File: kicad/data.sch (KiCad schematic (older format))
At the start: 46 parts, among them J2 USB_C, J3 XCVR_CAT_TTL, J4 FTDI header, J5 PTT choice, J6 XCVR_PTT, J7 XCVR_CAT_RS232, U3 SN65220, U4 Si8663AB-B-IS1, U5 FT232RL, U6 MAX3387ECUG+, U7 VOR1121B6T

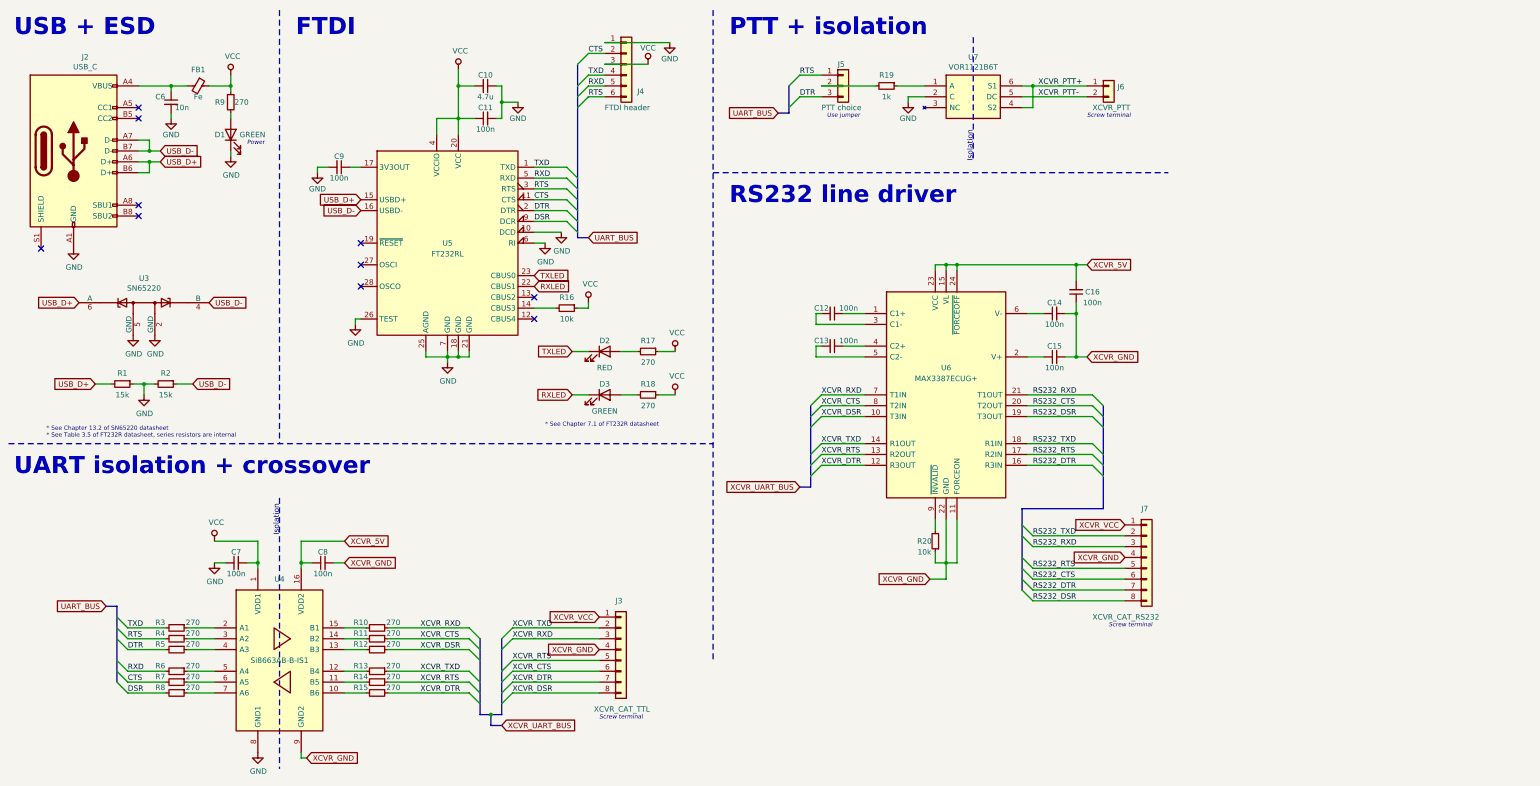
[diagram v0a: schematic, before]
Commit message: Filtering, jumpers, LEDs, misc
* Modified high level diagram to express the shared UART bus
* Renamed XCVR_VCC to XCVR_13V8
* Add solder jumpers on audio, PTT and UART lines for easy prototyping/bypassing
* Added bypass caps on XCVR side data and audio connectors
* Add series ferite beads on data ICs Vcc
* Added schottky diodes to all XCVR_13V8
* Changed series resistors of RXLED/TXLED/VccLED for 6mA current
* Added power LEDs on XCVR_13V8 connector terminals
* Added power LED for XCVR_5V rail
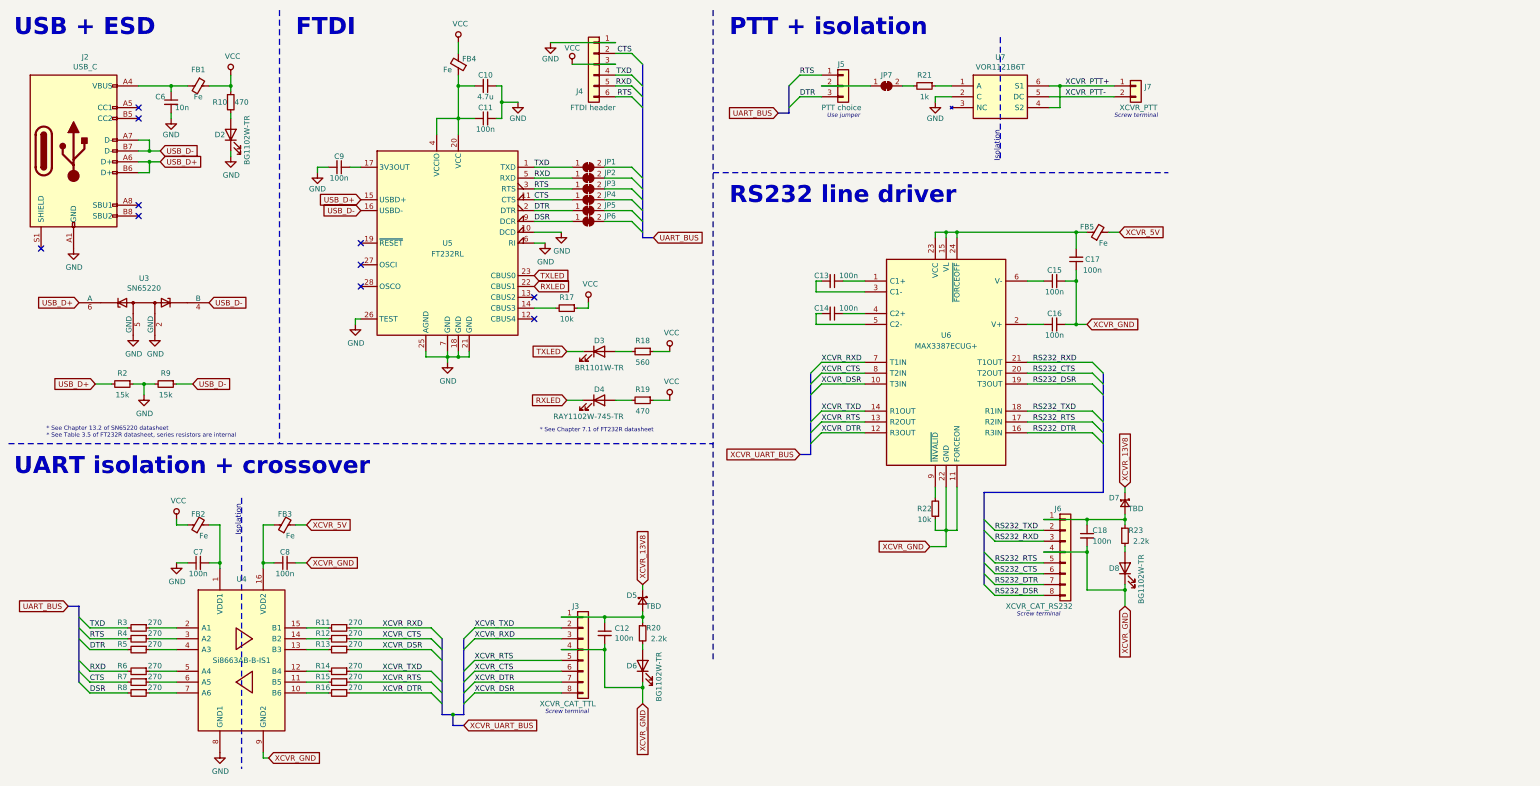
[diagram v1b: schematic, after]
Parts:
- added C12, C18: 100n, symbol Device:C_Small
- added D5, D7: TBD, symbol Device:D_Schottky_Small
- added D6, D8: BG1102W-TR, symbol Device:LED
- added FB2, FB3, FB4, FB5: Fe, symbol Device:Ferrite_Bead_Small
- added JP1, JP2, JP3, JP4, JP5, JP6, JP7: SolderJumper_2_Bridged, symbol Jumper:SolderJumper_2_Bridged
- added R20, R23: 2.2k, symbol Device:R_Small
- D2: renamed from D1; value GREEN -> BG1102W-TR
- D3: renamed from D2; value RED -> BR1101W-TR
- D4: renamed from D3; value GREEN -> RAY1102W-745-TR
- R10: renamed from R9; value 270 -> 470
- R18: renamed from R17; value 270 -> 560
- R19: renamed from R18; value 270 -> 470
- renumbered C12 to C13, C13 to C14, C14 to C15, C15 to C16, C16 to C17, J7 to J6, J6 to J7, R10 to R11, R11 to R12, R12 to R13, R13 to R14, R14 to R15, R15 to R16, R16 to R17, R1 to R2, R19 to R21, R20 to R22, R2 to R9
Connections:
- net CTS: now also JP4.1 (A)
- net DSR: now also JP6.1 (A)
- net DTR: now also JP5.1 (A)
- net RTS: now also JP3.1 (A)
- net RXD: now also JP2.1 (A)
- net TXD: now also JP1.1 (A)
- net VCC: now also FB2.1, FB4.2; no longer C10.2, C11.1, C7.2, U4.1 (VDD1), U5.20 (VCC), U5.4 (VCCIO)
- net XCVR_5V: now also FB3.2, FB5.2; no longer C17.2, C8.1, U4.16 (VDD2), U6.15 (VL), U6.23 (VCC), U6.24 (~FORCEOFF)
- net XCVR_GND: now also C12.2, C18.2, D6.1 (K), D8.1 (K)
- net at J5.2 (Pin_2): now also JP7.1 (A); no longer R21.2
- net XCVR_VCC: no longer names the net of J6.1 (Pin_1)
- net XCVR_VCC: now also C18.1, D7.2 (A), R23.1; no longer J3.1 (Pin_1)
- new net: C10.2, C11.1, FB4.1, U5.20 (VCC), U5.4 (VCCIO)
- new net: C12.1, D5.2 (A), J3.1 (Pin_1), R20.1
- new net: JP7.2 (B), R21.2
- new net: C17.2, FB5.1, U6.15 (VL), U6.23 (VCC), U6.24 (~FORCEOFF)
- new net: C7.2, FB2.2, U4.1 (VDD1)
- new net: C8.1, FB3.1, U4.16 (VDD2)
- new net: D8.2 (A), R23.2
- new net: D6.2 (A), R20.2
- new net XCVR_13V8: D5.1 (K), D7.1 (K)
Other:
- note removed: "Power"
- moved on the sheet: C13, C14, C15, C16, C17, C7, C8, D3, D4, J3, J4, J6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

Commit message: MAX driver protection
* Adjust label position for readability
* Protected R1OUT-R3OUT of MAX driver with OR gate
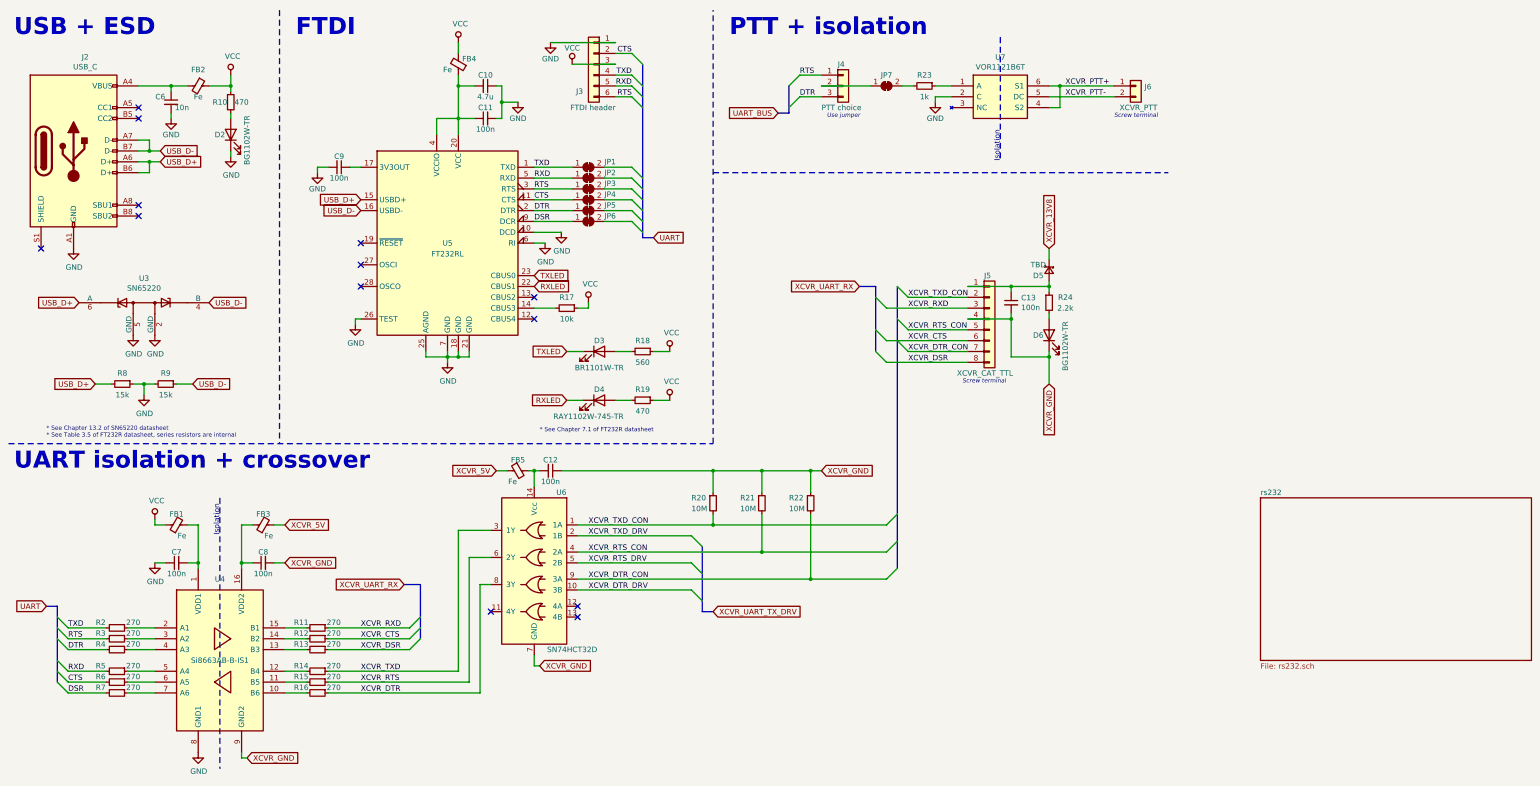
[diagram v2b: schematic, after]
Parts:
- removed C13, C14, C15, C16, C17, C18: 100n, symbol Device:C_Small
- removed D7: TBD, symbol Device:D_Schottky_Small
- removed D8: BG1102W-TR, symbol Device:LED
- removed J6: XCVR_CAT_RS232, symbol Connector_Generic:Conn_01x08
- removed R23: 2.2k, symbol Device:R_Small
- removed U6: MAX3387ECUG+, SOP65P640X110-24N, symbol custom:MAX3387ECUG+
- added C12: 100n, symbol Device:C_Small
- added R20, R21: 10M, symbol Device:R_Small
- added U6: SN74HCT32D, Package_SO:SOIC-14_3.9x8.7mm_P1.27mm, symbol custom:SN74HCT32D
- R22: value 10k -> 10M
- renumbered C12 to C13, FB2 to FB1, FB1 to FB2, J4 to J3, J5 to J4, J3 to J5, J7 to J6, R3 to R2, R21 to R23, R20 to R24, R4 to R3, R5 to R4, R6 to R5, R7 to R6, R8 to R7, R2 to R8
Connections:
- net XCVR_5V: now also FB5.1; no longer FB5.2
- net XCVR_DTR: now also U6.8 (3Y); no longer J5.7 (Pin_7)
- net XCVR_GND: now also C12.1, R20.1, R21.1, U6.7 (GND)
- net XCVR_RTS: now also U6.6 (2Y); no longer J5.5 (Pin_5)
- net XCVR_TXD: now also U6.3 (1Y); no longer J5.2 (Pin_2)
- net XCVR_DTR_CON: now reaches R22.2
- net XCVR_DTR_CON: now also J5.7 (Pin_7), U6.9 (3A)
- new net: C12.2, FB5.2, U6.14 (Vcc)
- new net XCVR_DTR_DRV: U6.10 (3B)
- new net XCVR_RTS_CON: J5.5 (Pin_5), R21.2, U6.4 (2A)
- new net XCVR_RTS_DRV: U6.5 (2B)
- new net XCVR_TXD_CON: J5.2 (Pin_2), R20.2, U6.1 (1A)
- new net XCVR_TXD_DRV: U6.2 (1B)
- no-connect marks 10 -> 13
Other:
- note removed: "RS232 line driver"
- moved on the sheet: C13, C7, C8, D5, D6, FB1, FB3, J5, R11, R12, R13, R14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

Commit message: Connector and pull down resistors
* Changed back to USB-B connector.
* Changed value of pull down resistors to 1k.
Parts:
- removed J2: USB_C, symbol Connector:USB_C_Receptacle_USB2.0
- added J2: USB_B, symbol Connector:USB_B
- R20, R21, R22: value 10M -> 1k
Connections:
- net GND: now also J2.4 (GND)
- net USB_D+: now also J2.2 (D-)
- net USB_D-: now also J2.3 (D+)
- net at C6.1, FB2.2: now also J2.1 (VBUS)
- no-connect marks 13 -> 9
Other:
- moved on the sheet: C6, D2, FB2, R10, R8, R9, U3

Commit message: Initial footprint placement + changes
* Added initial placement
* Remove pull-down resistors from USB lines.
* Remove ferrite bead from FTDI chip as it was very close to Vcc FB
* Fixed MAX TX pins
* Assigned footprints.
* Removed redundant solder jumpers.
* Small changes for layout coherence.
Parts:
- removed FB4: Fe, symbol Device:Ferrite_Bead_Small
- removed JP7: SolderJumper_2_Bridged, symbol Jumper:SolderJumper_2_Bridged
- removed R8, R9: 15k, symbol Device:R_Small
- added JP16, JP17: SolderJumper_2_Bridged, Jumper:SolderJumper-2_P1.3mm_Bridged_RoundedPad1.0x1.5mm, symbol Jumper:SolderJumper_2_Bridged
- C10, C11, C12, C13, C6, C7, C8, C9: footprint (none) -> Capacitor_SMD:C_1206_3216Metric_Pad1.42x1.75mm_HandSolder
- D2, D3, D4, D6: footprint (none) -> LED_SMD:LED_1206_3216Metric_Pad1.42x1.75mm_HandSolder
- D5: value TBD -> 1N4148X-TP; footprint (none) -> Diode_SMD:D_SOD-523
- FB1, FB2, FB3, FB5: footprint (none) -> Inductor_SMD:L_1206_3216Metric_Pad1.42x1.75mm_HandSolder
- J2: footprint (none) -> Connector_USB:USB_B_OST_USB-B1HSxx_Horizontal
- J3: footprint (none) -> Connector_PinHeader_2.54mm:PinHeader_1x06_P2.54mm_Vertical
- J4: footprint (none) -> Connector_PinHeader_2.54mm:PinHeader_1x03_P2.54mm_Vertical
- J5: footprint (none) -> custom:TB003-500-P08BE
- J6: footprint (none) -> custom:TB003-500-P02BE
- JP1, JP2, JP3, JP4, JP5, JP6: footprint (none) -> Jumper:SolderJumper-2_P1.3mm_Bridged_RoundedPad1.0x1.5mm
- R10, R11, R12, R13, R14, R15, R16, R17, R18, R19, R2, R20, R21, R22, R23, R24, R3, R4, R5, R6, R7: footprint (none) -> Resistor_SMD:R_1206_3216Metric_Pad1.42x1.75mm_HandSolder
- U3: footprint Package_TO_SOT_SMD:SOT-23-6 -> Package_TO_SOT_SMD:SOT-23-6_Handsoldering
- U4: footprint SOIC127P600X175-16N -> Package_SO:SOIC-16_3.9x9.9mm_P1.27mm
- U6: footprint Package_SO:SOIC-14_3.9x8.7mm_P1.27mm -> custom:SOIC-14_P1.27mm_Handsolder
- U7: footprint SOT254P980X380-6N -> Package_DIP:SMDIP-6_W9.53mm_Clearance8mm
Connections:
- net VCC: now also C10.2, C11.1, U5.20 (VCC), U5.4 (VCCIO)
- net XCVR_PTT-: now also JP17.2 (B); no longer U7.5 (DC)
- net at J4.2 (Pin_2): now also R23.2
- net XCVR_PTT+: no longer names the net of U7.4 (S2), U7.6 (S1)
- net XCVR_PTT+: now also JP16.1 (A); no longer J6.1 (Pin_1)
- new net: JP17.1 (A), U7.5 (DC)
- new net: J6.1 (Pin_1), JP16.2 (B)
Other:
- moved on the sheet: J6, R23, U7

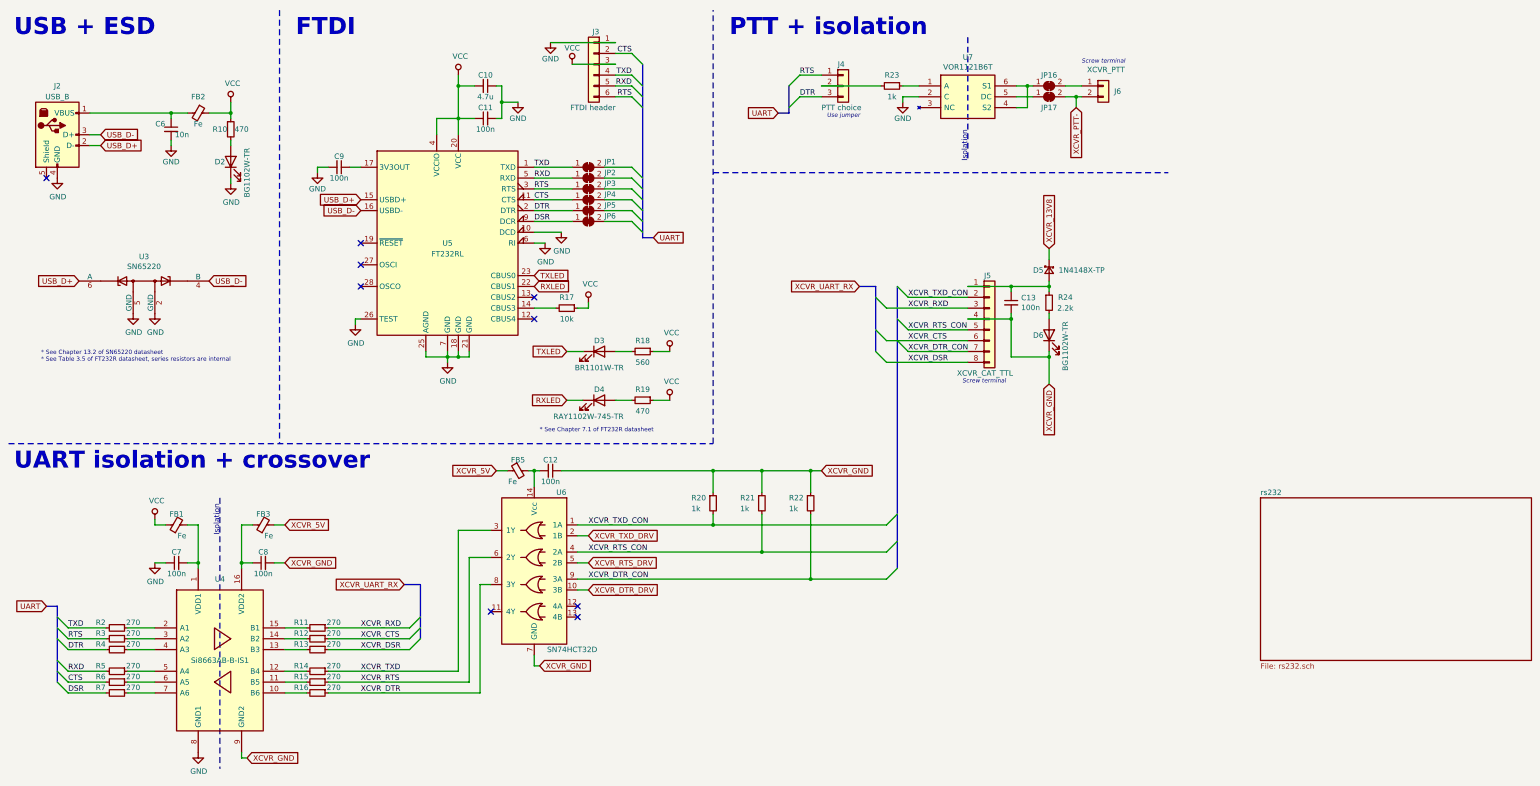
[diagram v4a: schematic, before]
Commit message: New layout, routing, misc...
* Redo layout
* Fixed MAX pulldown resistors on data lines.
* Added jumpers in case MAX not installed.
* Remove audio header
* Remove some redundant solder jumpers
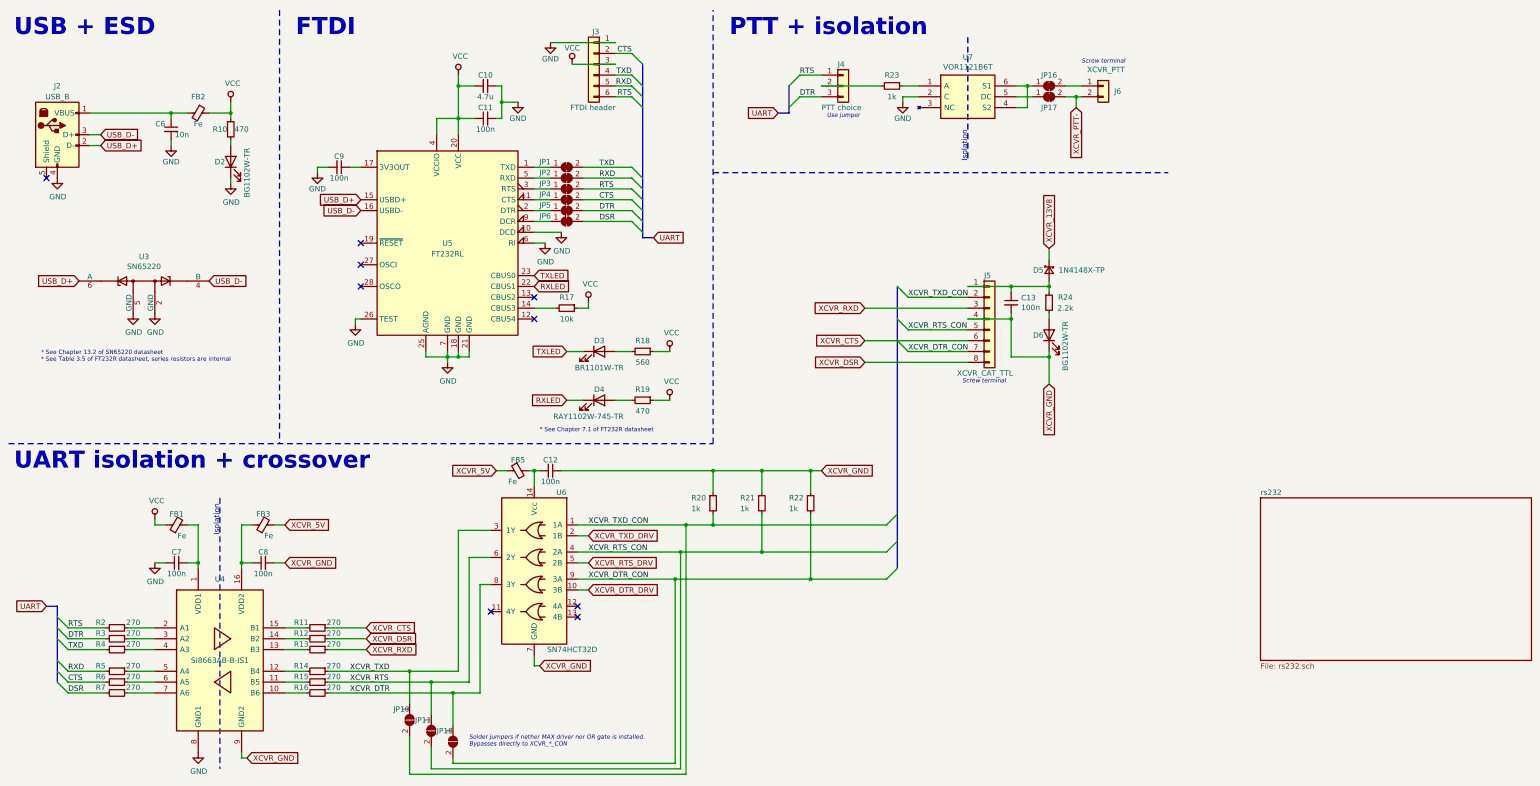
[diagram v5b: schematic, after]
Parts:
- added JP10, JP11, JP18: SolderJumper_2_Open, Jumper:SolderJumper-2_P1.3mm_Open_RoundedPad1.0x1.5mm, symbol Jumper:SolderJumper_2_Open
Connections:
- net CTS: now also JP4.2 (B); no longer JP4.1 (A), U5.11 (CTS)
- net DSR: now also JP6.2 (B); no longer JP6.1 (A), U5.9 (DCR)
- net DTR: now also JP5.2 (B), R3.2; no longer JP5.1 (A), R4.2, U5.2 (DTR)
- net RTS: now also JP3.2 (B), R2.2; no longer JP3.1 (A), R3.2, U5.3 (RTS)
- net RXD: now also JP2.2 (B); no longer JP2.1 (A), U5.5 (RXD)
- net TXD: now also JP1.2 (B), R4.2; no longer JP1.1 (A), R2.2, U5.1 (TXD)
- net XCVR_CTS: now also R11.1; no longer R12.1
- net XCVR_DSR: now also R12.1; no longer R13.1
- net XCVR_DTR: now also JP18.1 (A)
- net XCVR_DTR_CON: now also JP18.2 (B)
- net XCVR_RTS: now also JP11.1 (A)
- net XCVR_RTS_CON: now also JP11.2 (B)
- net XCVR_RXD: now also R13.1; no longer R11.1
- net XCVR_TXD: now also JP10.1 (A)
- net XCVR_TXD_CON: now also JP10.2 (B)
- new net: JP1.1 (A), U5.1 (TXD)
- new net: JP4.1 (A), U5.11 (CTS)
- new net: JP5.1 (A), U5.2 (DTR)
- new net: JP3.1 (A), U5.3 (RTS)
- new net: JP2.1 (A), U5.5 (RXD)
- new net: JP6.1 (A), U5.9 (DCR)
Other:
- note added: "Solder jumpers if nether MAX driver nor OR gate is installed.\nBypasses directly to XCVR_*_CON"
- moved on the sheet: JP1, JP2, JP3, JP4, JP5, JP6
